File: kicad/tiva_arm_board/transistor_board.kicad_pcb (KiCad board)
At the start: 2 copper layers, 25.4 x 38.1 mm, 16 parts, among them J1 Conn_01x10, Q1 Q_NIGBT_GCEC, Q2 Q_NIGBT_GCEC, Q3 MMBF170, Q4 MMBF170, U2 ESP32-cam, U3 LM7805_TO220

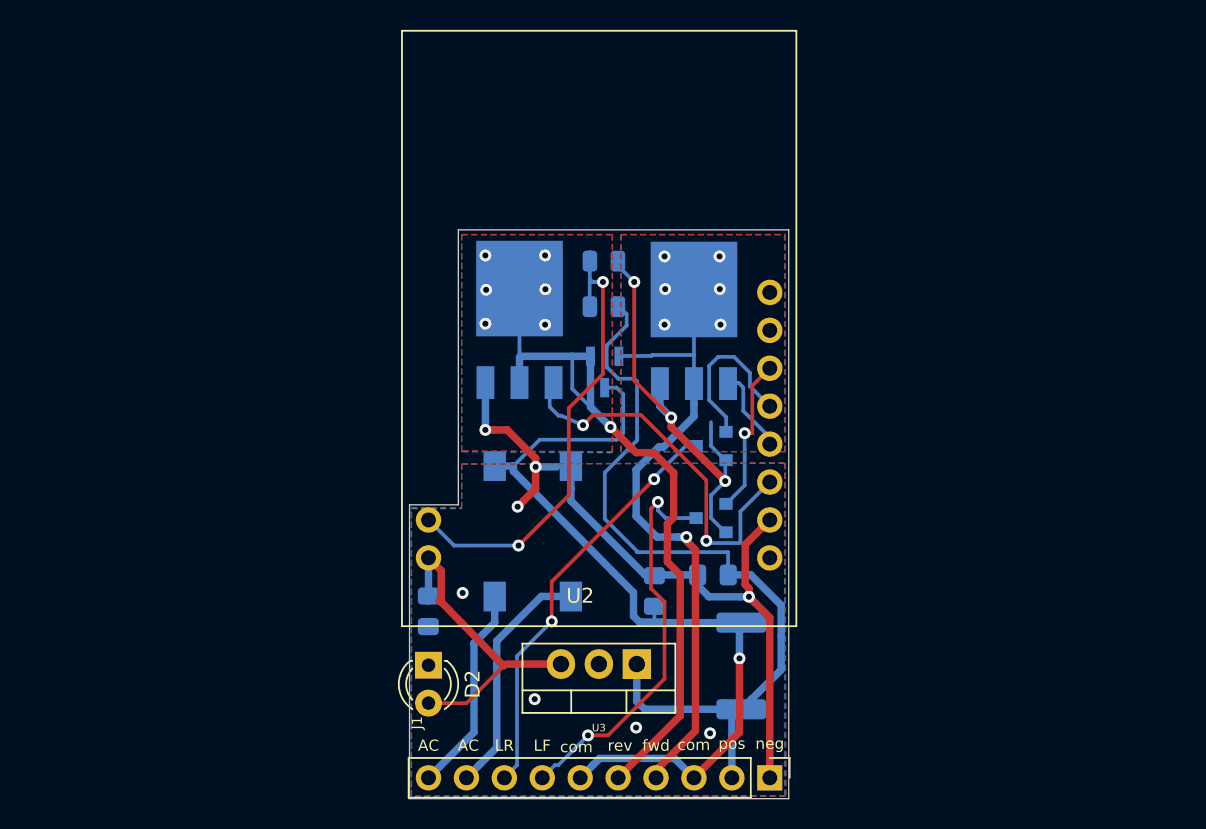
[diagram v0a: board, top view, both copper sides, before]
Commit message: corrected the transistors
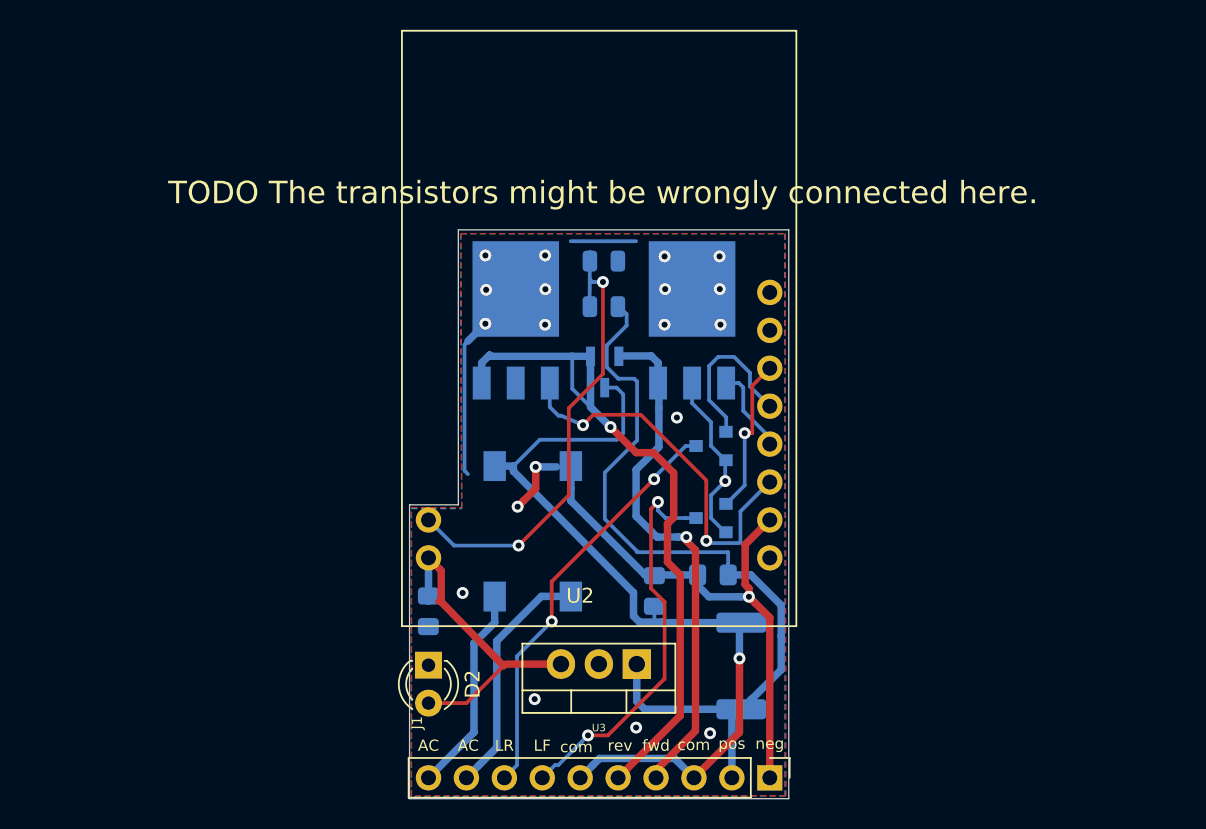
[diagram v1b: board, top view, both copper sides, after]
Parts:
- Q1, Q2: value Q_NIGBT_GCEC -> MMBF170
- moved Q1 11.9 mm to (120.1, 103.3)
- moved Q2 11.6 mm to (132.0, 103.3)
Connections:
- Q1 pad 2: Net-(D3-Pad2) -> GND
- Q1 pad 3: GND -> Net-(D3-Pad1)
- Q2 pad 2: Net-(D3-Pad1) -> GND
- Q2 pad 3: GND -> Net-(D3-Pad2)
- U2 pad 3: Net-(Q2-Pad1) -> Net-(Q1-Pad1)
- U2 pad 4: Net-(Q1-Pad1) -> Net-(Q2-Pad1)
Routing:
- net Net-(Q2-Pad1): track 25.8 -> 5.80 mm, vias 2 -> 0
- net Net-(Q1-Pad1): track 5.80 -> 25.8 mm, vias 0 -> 2
- net GND: track 78.7 -> 68.8 mm, vias 11 -> 21
- net Net-(D3-Pad2): track 43.4 -> 35.1 mm, vias 7 -> 1
- net Net-(D3-Pad1): track 49.1 -> 46.4 mm, vias 7 -> 1
- removed copper zone on B.Cu, net Net-(D3-Pad1)
- removed copper zone on F.Cu, net Net-(D3-Pad1)
- removed copper zone on B.Cu, net Net-(D3-Pad2)
- removed copper zone on F.Cu, net Net-(D3-Pad2)
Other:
- board text added: "TODO The transistors might be wrongly connected here."
